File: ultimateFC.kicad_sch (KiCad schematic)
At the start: 213 parts, among them J1 USB_B_Micro, SW1 SW_Push, U1 LMR33630CQRNX, U2 TPS62824ADMQ, U3 LMR33620CRNXT, U4 S25FL064L, U5 DPS310, U6 BMI270, U7 STM32H735VGH6, U8 ICM-20602, Y1 CSTNE8M00G550000R0

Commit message: MORE PADS!!!
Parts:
- added TP117, TP118, TP119, TP120, TP121, TP122, TP123, TP124, TP125, TP126, TP127, TP128, TP129, TP130, TP131, TP132, TP133, TP134, TP135, TP136, TP137, TP138, TP139, TP140, TP141, TP142, TP143: Pad, TestPoint:TestPoint_Pad_1.5x1.5mm, symbol Connector:TestPoint_Flag
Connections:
- net +3V3: now also TP123.1, TP129.1, TP136.1, TP141.1
- net +5V: now also TP121.1, TP122.1, TP132.1, TP133.1, TP135.1, TP142.1
- net GND: now also TP124.1, TP125.1, TP126.1, TP127.1, TP128.1, TP130.1, TP131.1, TP134.1, TP140.1, TP143.1
- net NRST: now also TP139.1
- net SWDCLK: now also TP138.1
- net SWDIO: now also TP137.1
- net USB_VBUS: now also TP118.1
- net USB_VBUS_sense: now also TP117.1
- net at J1.2 (D-), U7.D10 (PA11): now also TP119.1
- net at J1.3 (D+), U7.D9 (PA12): now also TP120.1
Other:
- moved on the sheet: C10, C12, C13, C14, C15, C16, C17, C18, C19, C20, C21, C22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

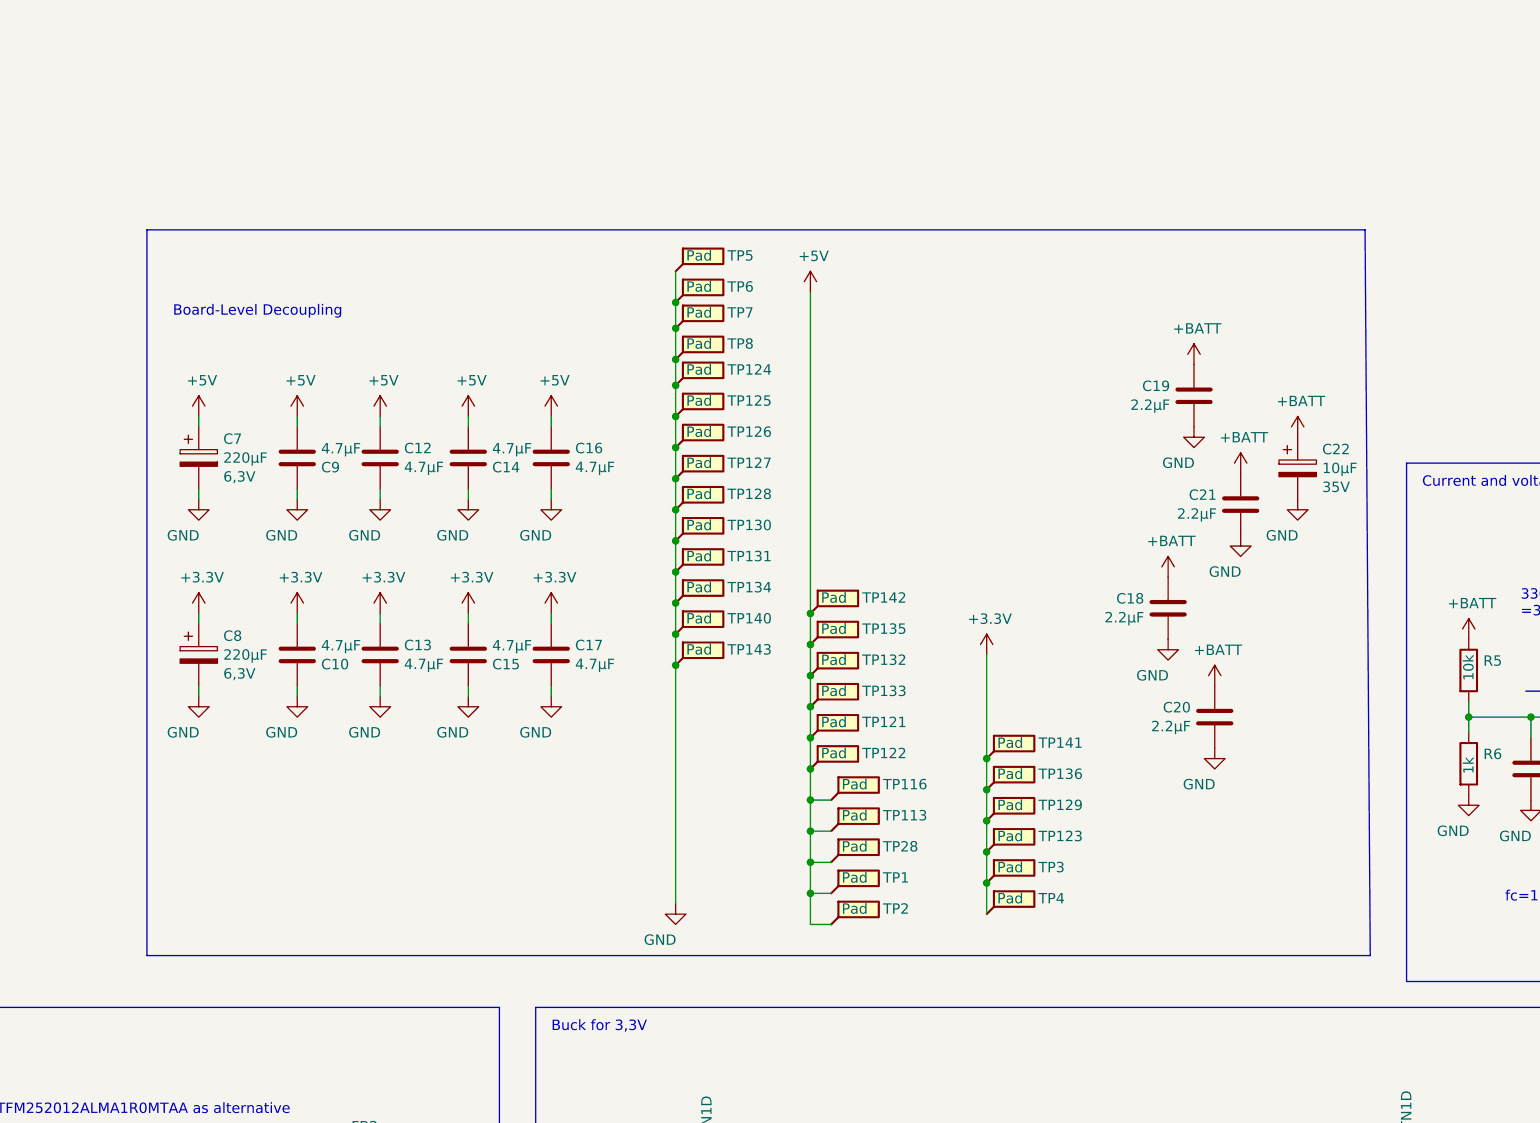
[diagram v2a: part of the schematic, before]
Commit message: add RF connectors
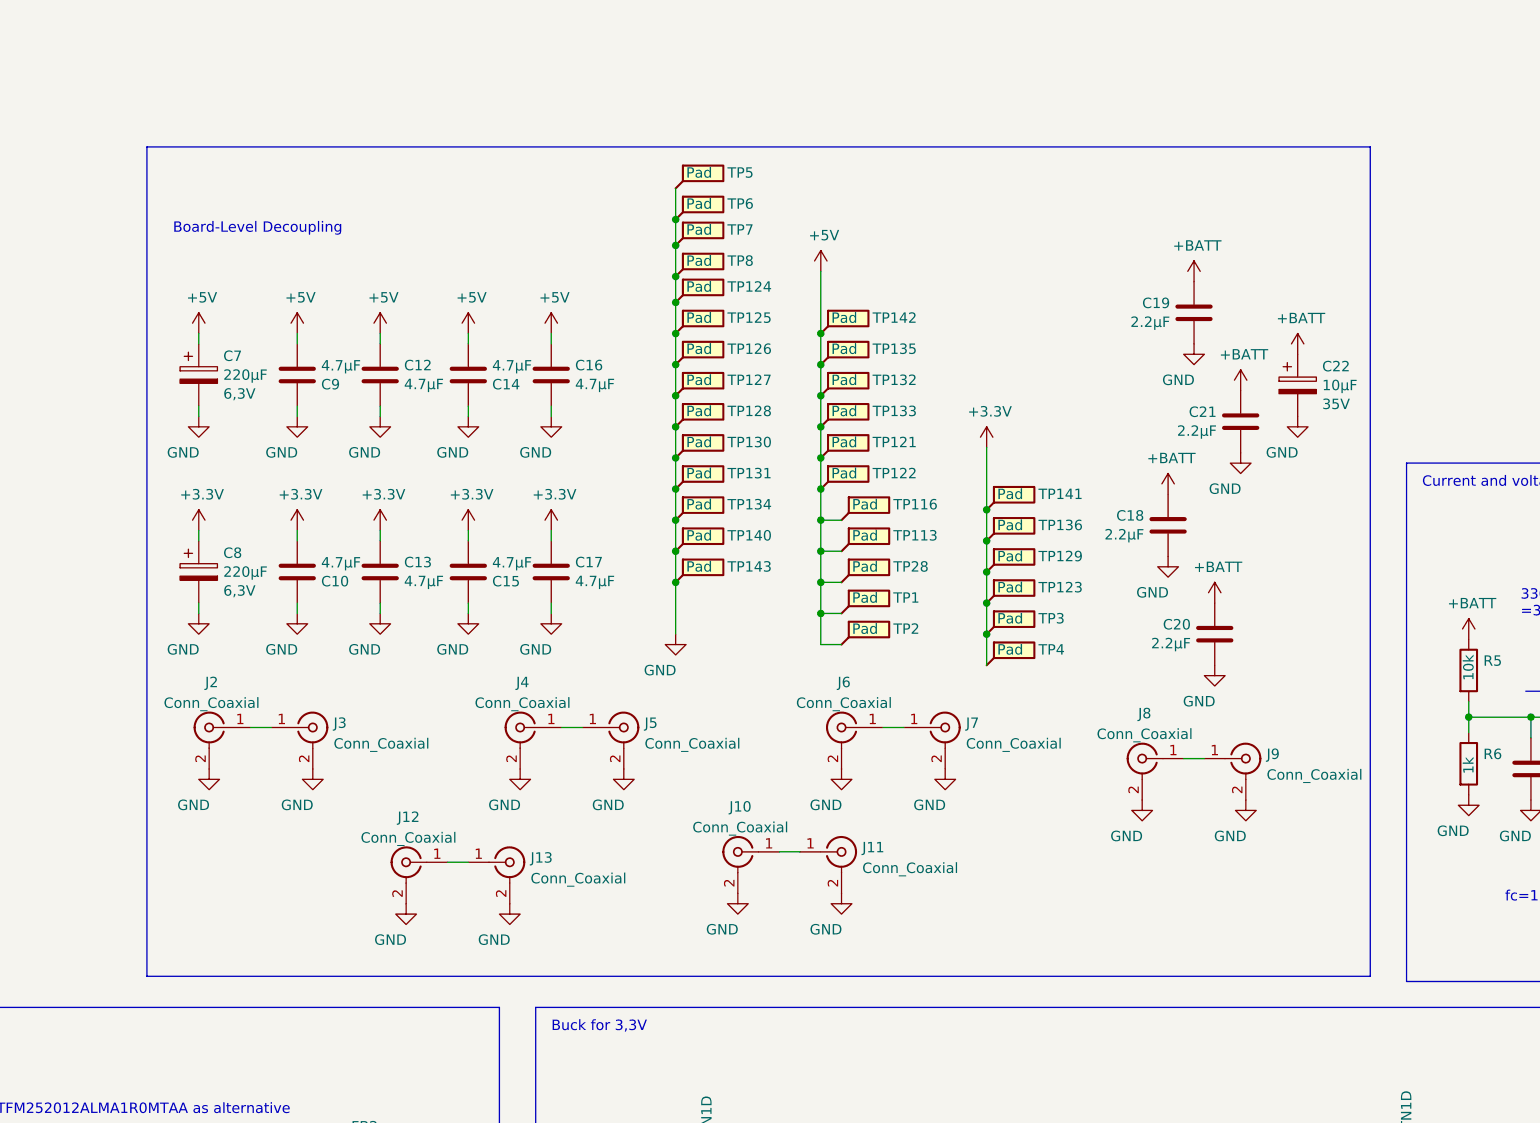
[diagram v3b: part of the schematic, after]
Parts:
- added J10, J11, J12, J13, J2, J3, J4, J5, J6, J7, J8, J9: Conn_Coaxial, ultimateFC:Amphenol_RF_A-4JA, symbol Connector:Conn_Coaxial
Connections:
- net GND: now also J10.2 (Ext), J11.2 (Ext), J12.2 (Ext), J13.2 (Ext), J2.2 (Ext), J3.2 (Ext), J4.2 (Ext), J5.2 (Ext), J6.2 (Ext), J7.2 (Ext), J8.2 (Ext), J9.2 (Ext)
- new net: J2.1 (In), J3.1 (In)
- new net: J12.1 (In), J13.1 (In)
- new net: J8.1 (In), J9.1 (In)
- new net: J4.1 (In), J5.1 (In)
- new net: J10.1 (In), J11.1 (In)
- new net: J6.1 (In), J7.1 (In)
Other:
- moved on the sheet: C10, C12, C13, C14, C15, C16, C17, C18, C19, C20, C21, C22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

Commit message: update layout
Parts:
- removed J10, J11, J12, J13, J6, J7: Conn_Coaxial, ultimateFC:Amphenol_RF_A-4JA, symbol Connector:Conn_Coaxial
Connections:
- net +3V3: now also J8.1 (In), J9.1 (In)
- net +5V: now also J4.1 (In), J5.1 (In)
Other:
- note added: "excluded from board"
- moved on the sheet: C10, C12, C13, C14, C15, C16, C17, C18, C19, C20, C21, C22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

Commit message: update layout
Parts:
- removed TP137, TP138, TP139, TP140, TP66: Pad, TestPoint:TestPoint_Pad_1.5x1.5mm, symbol Connector:TestPoint_Flag
- added C39: 4.7µF, Capacitor_SMD:C_0603_1608Metric, symbol Device:C
- SW1: footprint Button_Switch_SMD:SW_Push_1P1T_NO_CK_KMR2 -> Button_Switch_SMD:SW_Push_1P1T-SH_NO_CK_KMR2xxG
- TP141, TP65, TP67, TP88, TP89: footprint TestPoint:TestPoint_Pad_1.5x1.5mm -> ultimateFC:chonker_swd_pad
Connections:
- net GND: now also C39.1
- net at D5.1 (VDD), D6.1 (K): now also C39.2
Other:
- note added: "VALUE?"
- note removed: "Bottom MP Pins"
- note removed: "Internal Pullup on NRST: 30k...50k"
- moved on the sheet: C10, C12, C13, C14, C15, C16, C17, C18, C19, C20, C21, C22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

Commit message: change pads, add coax datasheet
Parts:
- TP1, TP100, TP101, TP102, TP103, TP104, TP105, TP106, TP107, TP108, TP109, TP110, TP112, TP113, TP115, TP116, TP121, TP122, TP123, TP124, TP125, TP126, TP127, TP128, TP129, TP130, TP131, TP132, TP133, TP134, TP135, TP136, TP14, TP142, TP143, TP15, TP16, TP17, TP2, TP28, TP3, TP33, TP34, TP35, TP36, TP37, TP38, TP39, TP4, TP40, TP41, TP42, TP43, TP44, TP45, TP46, TP47, TP48, TP49, TP5, TP50, TP51, TP52, TP53, TP54, TP55, TP56, TP57, TP58, TP59, TP6, TP60, TP61, TP62, TP63, TP64, TP7, TP71, TP72, TP73, TP74, TP75, TP76, TP77, TP78, TP79, TP8, TP80, TP81, TP82, TP83, TP84, TP85, TP86, TP87, TP90, TP91, TP92, TP93, TP94, TP95, TP96, TP97, TP98, TP99: footprint TestPoint:TestPoint_Pad_1.5x1.5mm -> ultimateFC:chonker_TestPoint_Pad_1.5x2.0mm
- TP10, TP11, TP114, TP117, TP118, TP119, TP12, TP120, TP13, TP18, TP19, TP22, TP23, TP24, TP25, TP26, TP27, TP29, TP30, TP31, TP32, TP68, TP69, TP70, TP9: footprint TestPoint:TestPoint_Pad_1.5x1.5mm -> ultimateFC:chonker_TestPoint_Pad_1.5x1.5mm

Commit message: Added Caps
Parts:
- removed C19: 2.2µF, Capacitor_SMD:C_0603_1608Metric, symbol Device:C
- added C12, C13, C16, C17, C5, C6: 4.7µF, Capacitor_SMD:C_0402_1005Metric, symbol Device:C
- C20: value 2.2µF -> 4.7µF; footprint Capacitor_SMD:C_0603_1608Metric -> Capacitor_SMD:C_0402_1005Metric; Dielektrikum X5R -> X7S; Mfr.No: GRM188R6YA475KE15D -> LLA215C70G105MA14K; Spannung 35V -> 6,3V; price@100[€] 0,11 -> 0,149; price@10[€] 0,113 -> 0,248; price@1k[€] 0,104 -> 0,066
- C21: value 2.2µF -> 4.7µF; footprint Capacitor_SMD:C_0603_1608Metric -> Capacitor_SMD:C_0402_1005Metric; Dielektrikum X5R -> X7S; Mfr.No: GRM188R6YA475KE15D -> LLA219C70G225MA01L; Spannung 35V -> 4V; price@100[€] 0,11 -> 0,127; price@10[€] 0,113 -> 0,213; price@1k[€] 0,104 -> 0,066
- renumbered C22 to C1, C18 to C10, C3 to C11, C9 to C14, C13 to C15, C12 to C18, C15 to C19, C7 to C2, C16 to C22, C10 to C23, C4 to C24, C5 to C25, C6 to C26, C11 to C27, C23 to C28, C24 to C29, C8 to C3, C25 to C30, C26 to C31, C27 to C32, C28 to C33, C29 to C34, C30 to C35, C31 to C36, C32 to C37, C33 to C38, C34 to C39, C1 to C4, C39 to C40, C35 to C41, C36 to C42, C37 to C43, C38 to C44, C14 to C7, C17 to C8, C2 to C9, D6 to D2, D5 to D3, D2 to D4, D3 to D5, D4 to D6, J2 to J1, J3 to J2, J4 to J3, J5 to J4, J8 to J5, J9 to J6, J1 to J7, R28 to R11, R11 to R12, R22 to R13, R18 to R14, R19 to R15, R20 to R16, R21 to R17, R12 to R18, R13 to R19, R14 to R20, R15 to R21, R16 to R22, R17 to R23, R23 to R24, R24 to R25, R25 to R26, R26 to R27, R27 to R28, TP5 to TP1, TP130 to TP10, TP78 to TP100, TP79 to TP101, TP80 to TP102, TP81 to TP103, TP82 to TP104, TP83 to TP105, TP84 to TP106, TP85 to TP107, TP86 to TP108, TP87 to TP109, TP131 to TP11, TP88 to TP110, TP89 to TP111, TP90 to TP112, TP91 to TP113, TP92 to TP114, TP93 to TP115, TP94 to TP116, TP95 to TP117, TP96 to TP118, TP97 to TP119, TP134 to TP12, TP98 to TP120, TP99 to TP121, TP100 to TP122, TP101 to TP123, TP102 to TP124, TP103 to TP125, TP104 to TP126, TP105 to TP127, TP106 to TP128, TP107 to TP129, TP143 to TP13, TP108 to TP130, TP109 to TP131, TP110 to TP132, TP69 to TP133, TP70 to TP134, TP117 to TP135, TP119 to TP136, TP120 to TP137, TP118 to TP138, TP142 to TP14, TP135 to TP15, TP132 to TP16, TP133 to TP17, TP121 to TP18, TP122 to TP19, TP6 to TP2, TP116 to TP20, TP113 to TP21, TP28 to TP22, TP1 to TP23, TP2 to TP24, TP141 to TP25, TP136 to TP26, TP129 to TP27, TP123 to TP28, TP3 to TP29, TP7 to TP3, TP4 to TP30, TP9 to TP31, TP10 to TP32, TP11 to TP33, TP12 to TP34, TP13 to TP35, TP111 to TP36, TP114 to TP37, TP14 to TP38, TP15 to TP39, TP8 to TP4, TP16 to TP40, TP17 to TP41, TP115 to TP42, TP18 to TP43, TP19 to TP44, TP29 to TP45, TP30 to TP46, TP31 to TP47, TP32 to TP48, TP22 to TP49, TP124 to TP5, TP23 to TP50, TP24 to TP51, TP25 to TP52, TP26 to TP53, TP27 to TP54, TP65 to TP55, TP33 to TP56, TP34 to TP57, TP35 to TP58, TP36 to TP59, TP125 to TP6, TP37 to TP60, TP38 to TP61, TP39 to TP62, TP40 to TP63, TP41 to TP64, TP42 to TP65, TP43 to TP66, TP44 to TP67, TP45 to TP68, TP46 to TP69, TP126 to TP7, TP47 to TP70, TP48 to TP71, TP49 to TP72, TP50 to TP73, TP51 to TP74, TP52 to TP75, TP53 to TP76, TP54 to TP77, TP55 to TP78, TP56 to TP79, TP127 to TP8, TP57 to TP80, TP58 to TP81, TP59 to TP82, TP60 to TP83, TP61 to TP84, TP62 to TP85, TP63 to TP86, TP64 to TP87, TP67 to TP88, TP112 to TP89, TP128 to TP9, TP20 to TP90, TP21 to TP91, TP68 to TP92, TP71 to TP93, TP72 to TP94, TP73 to TP95, TP74 to TP96, TP75 to TP97, TP76 to TP98, TP77 to TP99, U7 to U6, U8 to U7, U6 to U8
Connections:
- net +3V3: now also C21.2, C13.1, C17.2, C6.1
- net +5V: now also C20.1, C12.2, C16.1, C5.2
- net +BATT: no longer C20.1, C21.1
- net GND: now also C21.1, C12.1, C13.2, C16.2, C17.1, C5.1, C6.2; no longer C21.2

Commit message: update layout, labels, silkscreen
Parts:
- TP1, TP18, TP21, TP22, TP23, TP24, TP29, TP3, TP30, TP38, TP4, TP40, TP41, TP6, TP7: footprint ultimateFC:chonker_TestPoint_Pad_1.5x2.0mm -> ultimateFC:chonker_pwr_pad
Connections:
- net +10V: no longer TP39.1
- net +3V3: no longer TP27.1, TP28.1
- net +5V: no longer TP14.1, TP15.1, TP16.1, TP17.1, TP19.1
- net GND: no longer TP10.1, TP11.1, TP12.1, TP13.1, TP9.1
- net USB_DP: now reaches J7.2 (D-), TP136.1, U6.D10 (PA11)
- net USB_DM: now reaches J7.3 (D+), TP137.1, U6.D9 (PA12)
- net PB8: now reaches TP64.1, U6.A4 (PB8)
- net BOOT0: now reaches R12.1, SW1.1, U6.A5 (BOOT0)
- net BOOT0: now also TP16.1
- net PB5: now reaches TP61.1, U6.A6 (PB5)
- net PD3: now reaches TP75.1, U6.A8 (PD3)
- net PD2: now reaches TP74.1, U6.A9 (PD2)
- net PB3: now reaches TP59.1, U6.B6 (PB3)
- net PD4: now reaches TP76.1, U6.B7 (PD4)
- net PD1: now reaches TP73.1, U6.B8 (PD1)
- net PB4: now reaches TP60.1, U6.C5 (PB4)
- net PD7: now reaches TP79.1, U6.C6 (PD7)
- net PD0: now reaches TP72.1, U6.C7 (PD0)
- net PB9: now reaches TP65.1, U6.E3 (PB9)
- net IMU_INT2A: now reaches TP123.1, U6.H6 (PE10)
- net PB2: now reaches TP58.1, U6.J5 (PB2)
- net CS_GYRO renamed PA15_CS_20602
- net CS_OSD renamed PB12_CS_270
- net ESC_3_TX renamed PD12
- net ESC_4_TX renamed PD13
- net I2C_SCL renamed PB10_I2C2_SCL
- net I2C_SDA renamed PB11_I2C2_SDA
- net IMU_INT1A renamed PD10_IMU_INT1A
- net IMU_INT1B renamed PD11_IMU_INT1B
- net MISO_FLASH renamed MISO_SPI4
- net MISO_GYRO renamed MISO_SPI3
- net MISO_OSD renamed PB14_MISO_SPI2
- net MOSI_FLASH renamed MOSI_SPI4
- net MOSI_GYRO renamed MOSI_SPI3
- net MOSI_OSD renamed PB15_MOSI_SPI2
- net MOTOR1 renamed PC6_MOTOR1
- net MOTOR2 renamed PC9_MOTOR2
- net MOTOR3 renamed PC8_MOTOR3
- net MOTOR4 renamed PC7_MOTOR4
- net MP_PIN1 renamed PB0
- net MP_PIN4 renamed PB1
- net MP_PIN5 renamed PB6
- net MP_PIN6 renamed PB7
- net SCLK_FLASH renamed SCLK_SPI4
- net SCLK_GYRO renamed SCLK_SPI3
- net SCLK_OSD renamed PB13_SCLK_SPI2
- net UART2_RX renamed PD6_UART2_RX
- net UART2_TX renamed PD5_UART2_TX
- net UART3_RX renamed PD9_UART3_RX
- net UART3_TX renamed PD8_UART3_TX
- net UART9_RX renamed PD15_UART9_RX
- net UART9_TX renamed PD14_UART9_TX
- net curr_sig renamed PA5_curr_sig
- net vol_sig renamed PC5_vol_sig
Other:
- note removed: "B00 - TIM3_CH3 (ADC12_INP9)"
- note removed: "B01 - TIM3_CH4 (ADC12_INP5)"
- note removed: "B06 - TIM4_CH1"
- note removed: "B07 - TIM4_CH2"
- note removed: "FIX POWER"
- note removed: "TIM4_CH1"
- note removed: "TIM4_CH2"
- note removed: "Top MP Pins"
- note removed: "Video connector MP Pins"
- moved on the sheet: TP10, TP100, TP101, TP102, TP103, TP104, TP105, TP106, TP107, TP11, TP12, TP13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
